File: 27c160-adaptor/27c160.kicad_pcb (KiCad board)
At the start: 2 copper layers, 47 x 99.7 mm, 6 parts, among them P1 A19, P2 A18, U1 27C4096, U2 27C160

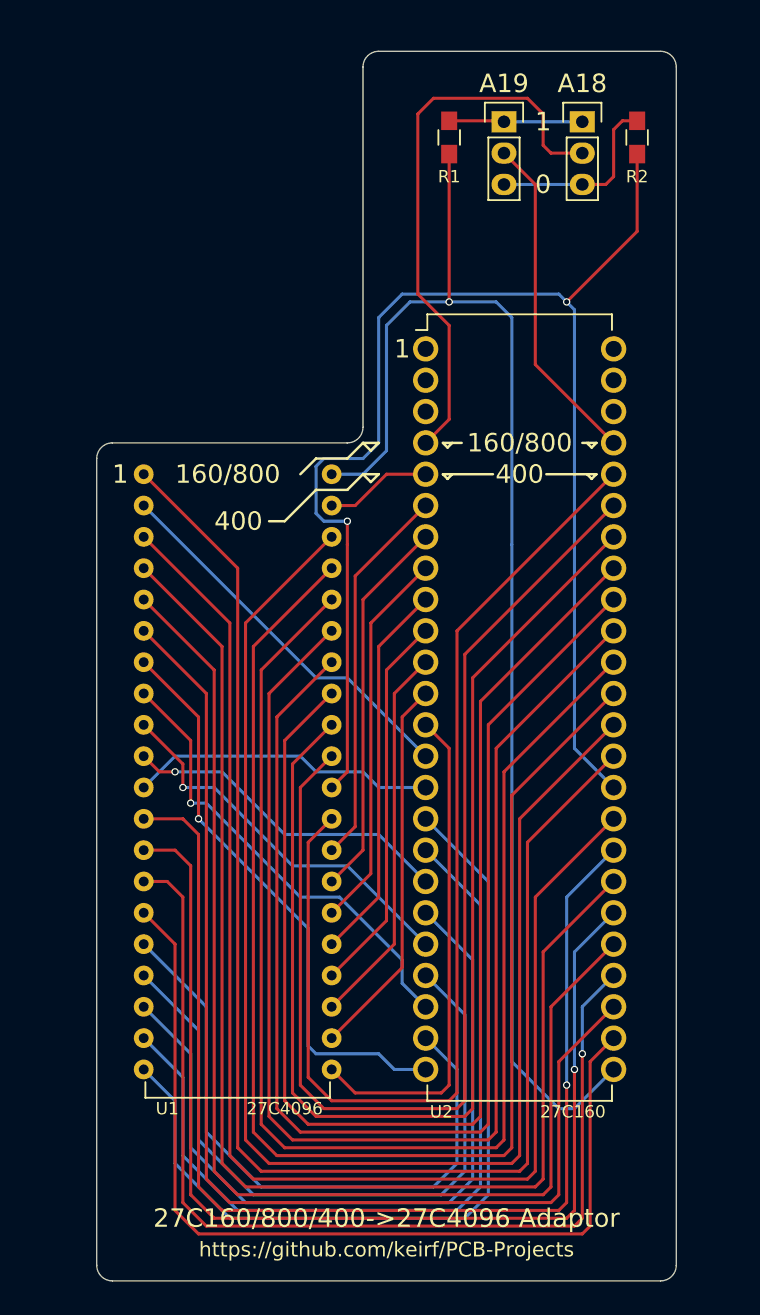
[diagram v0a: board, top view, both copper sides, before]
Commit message: made a THT version for easier soldering
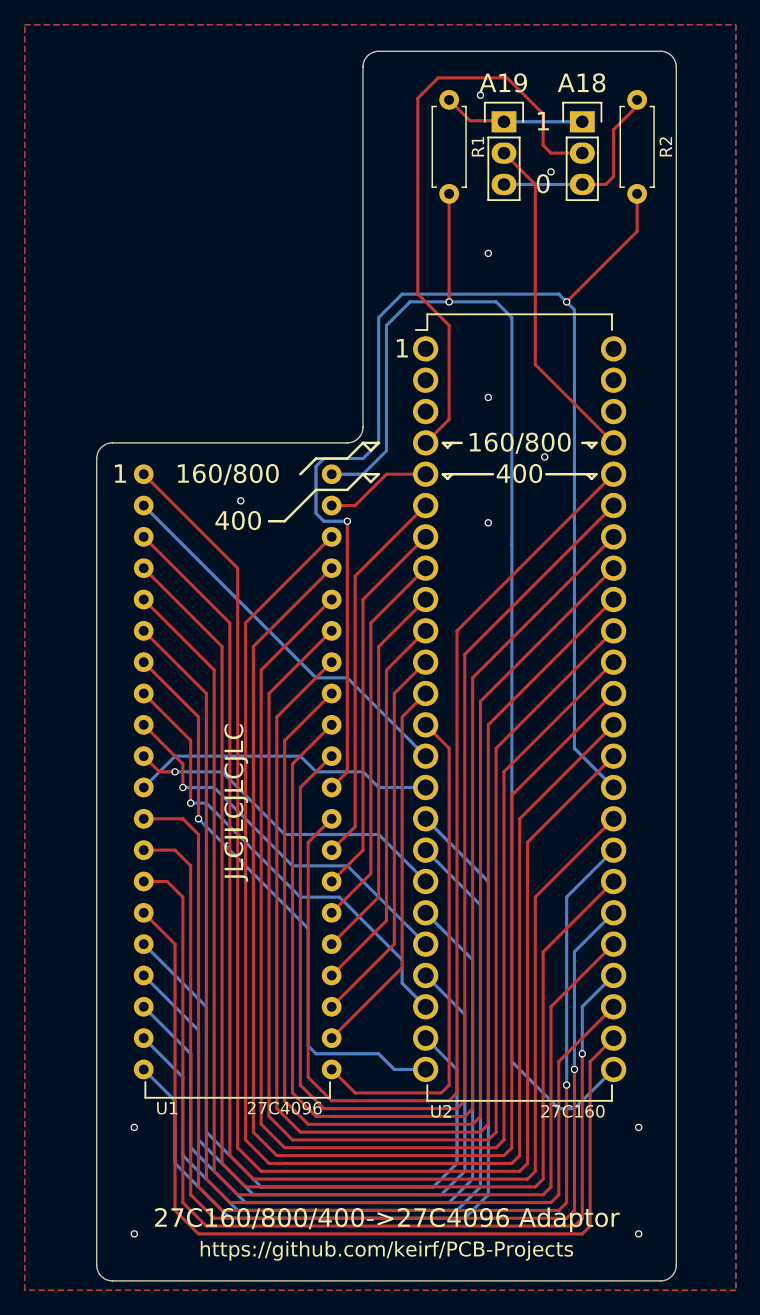
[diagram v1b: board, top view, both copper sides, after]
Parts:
- R1, R2: footprint Resistors_SMD:R_0805_HandSoldering -> Resistor_THT:R_Axial_DIN0207_L6.3mm_D2.5mm_P7.62mm_Horizontal
- moved R1 3.05 mm to (142.9, 33.8)
- moved R2 3.05 mm to (158.1, 33.8)
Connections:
- U2 pad 1: Net-(U2-Pad1) -> (no net)
- U2 pad 2: Net-(U2-Pad2) -> (no net)
- U2 pad 3: Net-(U2-Pad3) -> (no net)
- U2 pad 46: Net-(U2-Pad46) -> (no net)
- U2 pad 47: Net-(U2-Pad47) -> (no net)
- U2 pad 48: Net-(U2-Pad48) -> (no net)
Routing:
- net /VSS: track 116.4 -> 113.1 mm, vias 2 -> 13
- net /VCC: track 110.3 -> 107.1 mm
- net /A18: track 45.7 -> 47.8 mm
- net Net-(P1-Pad3): track 15.2 -> 16.2 mm
- net Net-(P1-Pad1): track 10.8 -> 11.5 mm
- added copper zone on B.Cu, net /VSS
- added copper zone on F.Cu, net /VSS
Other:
- board text added: "JLCJLCJLCJLC"
